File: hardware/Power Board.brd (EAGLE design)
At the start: 29 x 10 mm, 11 parts, among them J1 USB-MICRO-B, U1 MAX1555, U2 MCP1603T-330I/OS, X1 Battery 150mAh, X2 Output

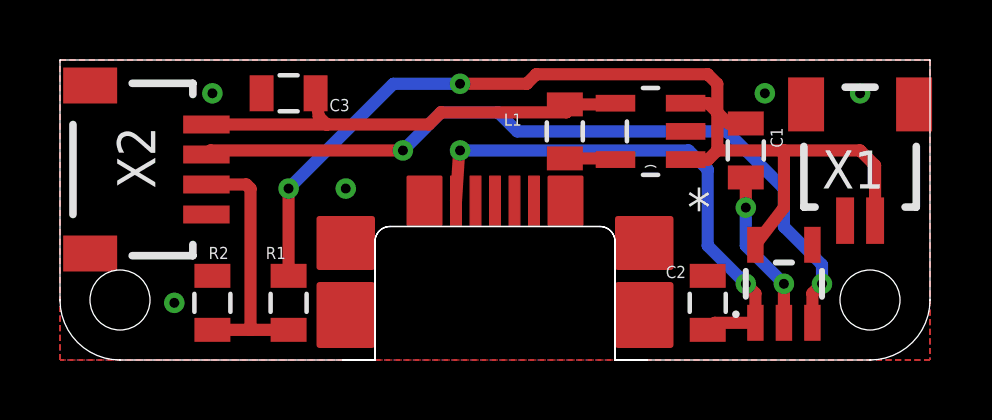
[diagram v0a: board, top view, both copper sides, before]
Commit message: Add bitmaps and python code to turn them into valid C++
This python is an abomination 🙃🐍
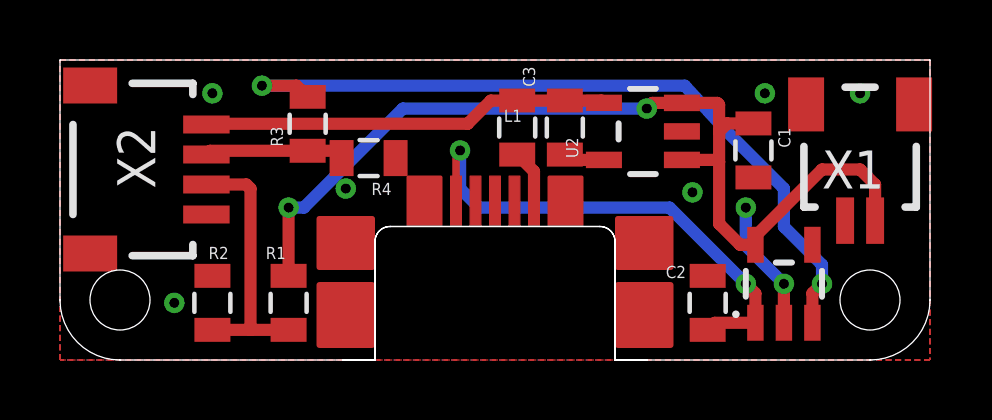
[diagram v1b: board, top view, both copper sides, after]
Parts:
- added R3, R4: 10kΩ, SparkFun-Passives:0805
- R1, R2: value (none) -> 10kΩ
- U2: value MCP1603T-330I/OS -> LM3671; device Microchip_By_element14_Batch_1:SOT95P280X110-5N -> texas-custom:SOT23-5
- moved C3 7.71 mm to (15.2, 7.75), turned to 270 degrees
- moved C1 0.25 mm to (23.1, 6.99)
- moved U2 0.25 mm to (19.4, 7.62), turned to 90 degrees
- moved L1 0.13 mm to (16.8, 7.75)
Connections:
- new net CHG_2: R3.1, R4.2, X2.2
- net CHG: now also R3.2; no longer X2.2
- net GND: now also R4.1
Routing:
- net CHG_2: track 0.00 -> 4.66 mm
- net V_BATT: track 35.4 -> 32.7 mm
- net VCC: track 15.3 -> 13.6 mm
- net GND: track 5.37 -> 6.15 mm, vias 7 -> 8
- net V_USB: track 17.7 -> 17.0 mm
